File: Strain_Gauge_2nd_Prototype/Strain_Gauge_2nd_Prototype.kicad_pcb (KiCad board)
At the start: 2 copper layers, 91 parts, among them J1 TC2030, J10 2601-1104, J11 Molex_104031-0811, J2 Conn_01x04, J3 Conn_01x04, J4 Conn_01x04, J5 Conn_01x04, J6 Conn_01x04, J7 Conn_01x04, J8 Conn_01x04, J9 USB4105-GF-A-060, Q1 PMV100EPA, SW1 SW_Push, U1 ADS131M08xPBS, U2 STM32F446RETx, U3 TPS73733DCQ, U4 MCP2562-E-SN, U5 LMR33610ADDAR, U6 TPS2113APWR, Y1 7XL-8.192MBD-T

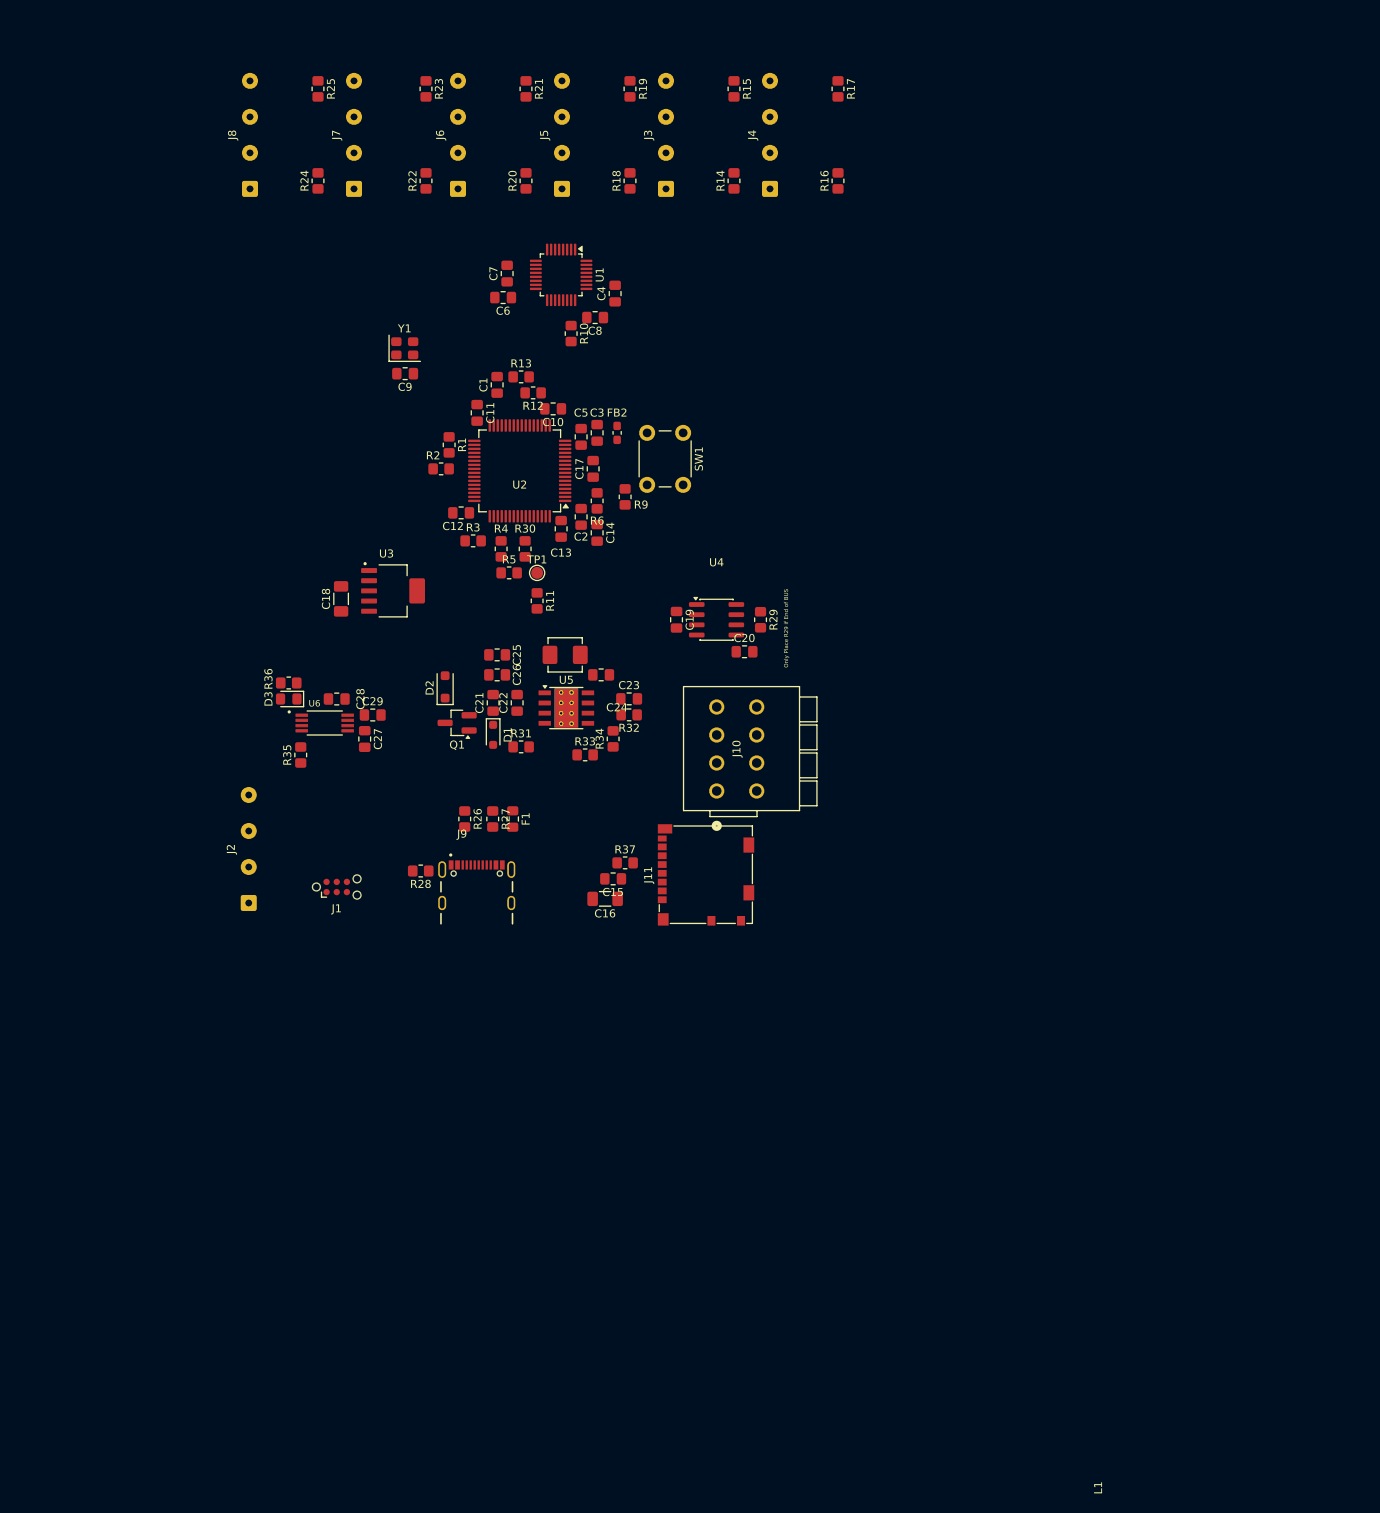
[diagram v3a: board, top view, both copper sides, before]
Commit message: Have redone the design, should be close to be routing. May just need to change the size of the 1uF capacitors down to get them closer to the ADS?
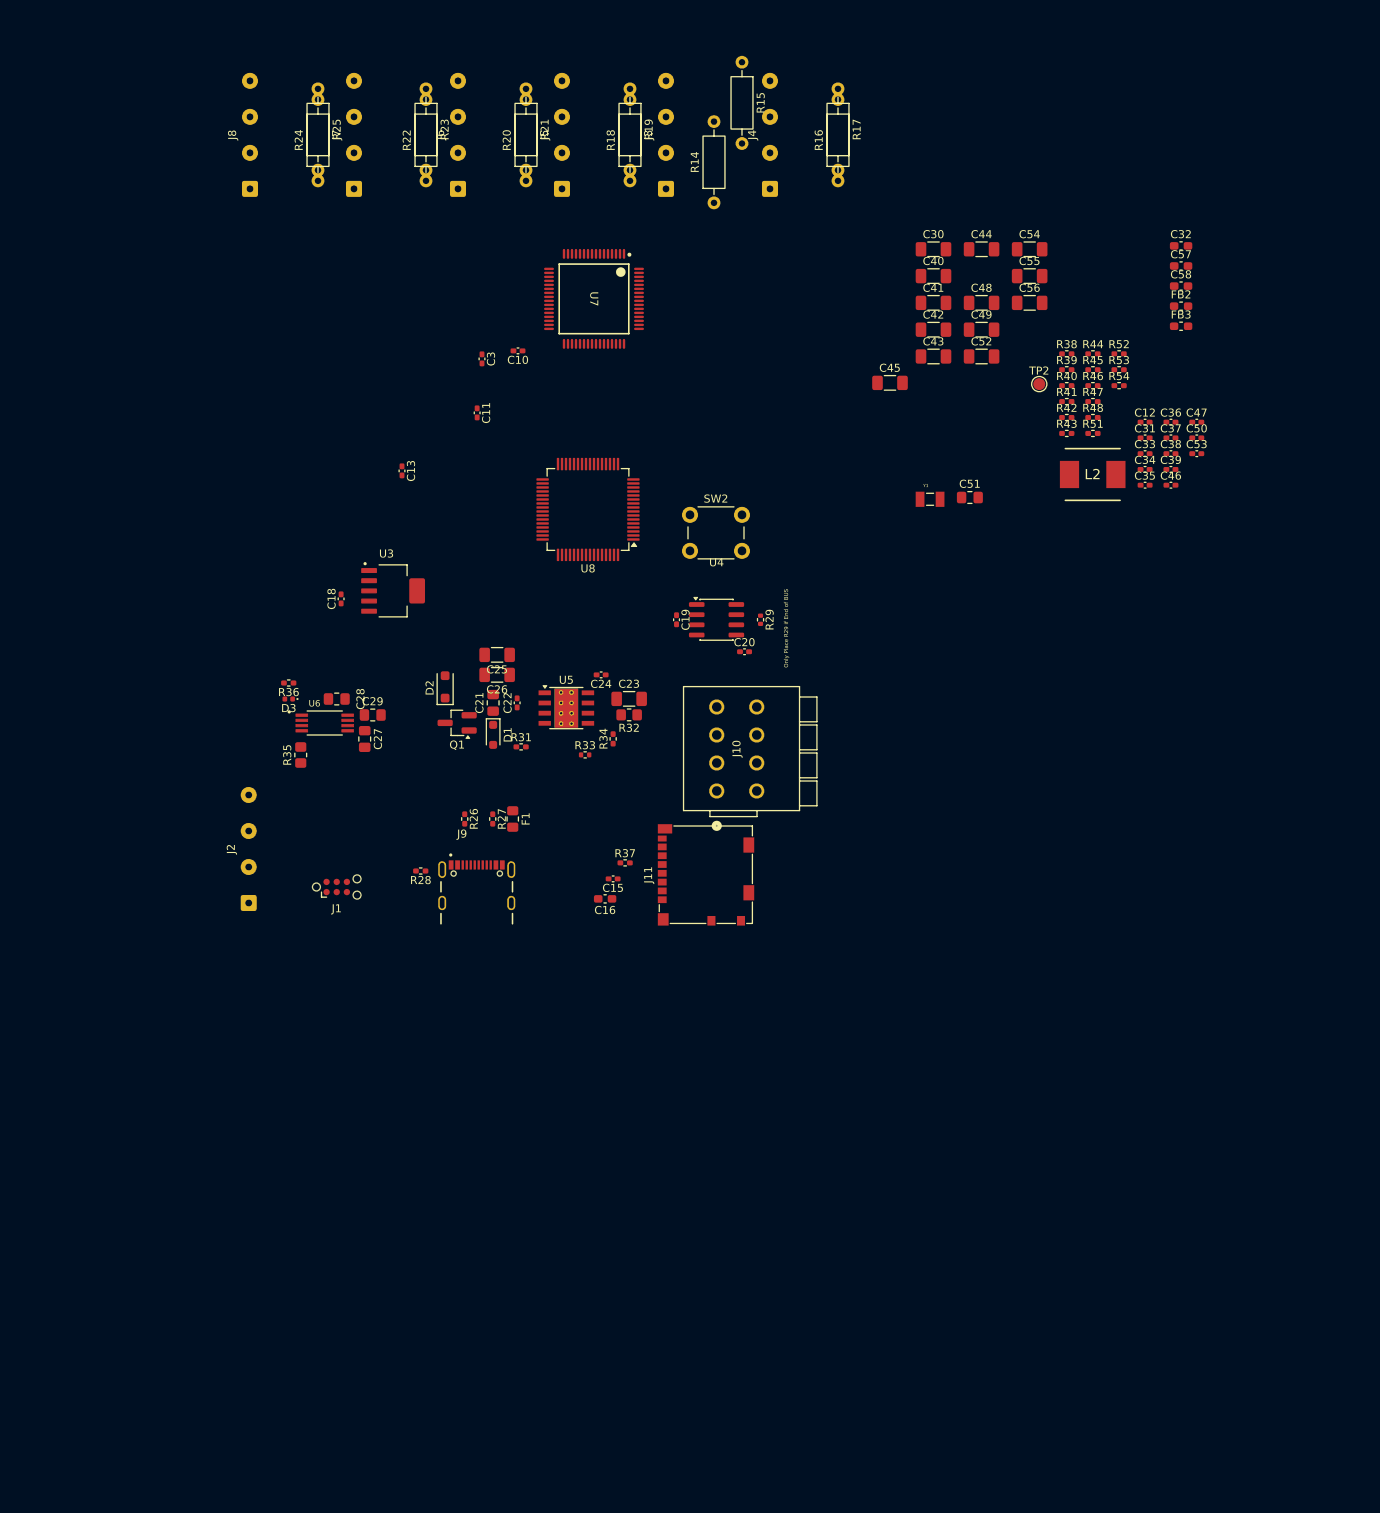
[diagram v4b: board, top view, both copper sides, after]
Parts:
- removed C1, C14: 4.7microF, Capacitor_SMD:C_0805_2012Metric_Pad1.18x1.45mm_HandSolder
- removed C17, C2, C7, C9: 100nF, Capacitor_SMD:C_0805_2012Metric_Pad1.18x1.45mm_HandSolder
- removed C4, C5, C6: 1microF, Capacitor_SMD:C_0805_2012Metric_Pad1.18x1.45mm_HandSolder
- removed C8: 220nF, Capacitor_SMD:C_0805_2012Metric_Pad1.18x1.45mm_HandSolder
- removed L1: 8.2uH, 86m, Inductor_SMD:L_Vishay_IHLP-1616
- removed R1, R11, R12, R13, R2, R3, R30, R4, R5, R6: 10k, Resistor_SMD:R_0805_2012Metric_Pad1.20x1.40mm_HandSolder
- removed R10, R9: 33, Resistor_SMD:R_0805_2012Metric_Pad1.20x1.40mm_HandSolder
- removed SW1: SW_Push, Button_Switch_THT:SW_PUSH_6mm
- removed TP1: TestPoint, TestPoint:TestPoint_Pad_D1.5mm
- removed U1: ADS131M08xPBS, Package_QFP:TQFP-32_5x5mm_P0.5mm
- removed U2: STM32F446RETx, Package_QFP:LQFP-64_10x10mm_P0.5mm
- added C30: 1microF, Capacitor_SMD:C_1206_3216Metric_Pad1.33x1.80mm_HandSolder, F.Cu at (172.9, 62.8)
- added C31: 100nF - VDDUSB, Capacitor_SMD:C_0402_1005Metric_Pad0.74x0.62mm_HandSolder, F.Cu at (199.4, 86.4)
- added C32: 4.7microF - General all board one, Capacitor_SMD:C_0603_1608Metric_Pad1.08x0.95mm_HandSolder, F.Cu at (203.9, 62.4)
- added C33: 100nF, Capacitor_SMD:C_0402_1005Metric_Pad0.74x0.62mm_HandSolder, F.Cu at (199.4, 88.3)
- added C34: 100nF, Capacitor_SMD:C_0402_1005Metric_Pad0.74x0.62mm_HandSolder, F.Cu at (199.4, 90.3)
- added C35: 100nF, Capacitor_SMD:C_0402_1005Metric_Pad0.74x0.62mm_HandSolder, F.Cu at (199.4, 92.3)
- added C36: 100nF, Capacitor_SMD:C_0402_1005Metric_Pad0.74x0.62mm_HandSolder, F.Cu at (202.6, 84.4)
- added C37: 100nF, Capacitor_SMD:C_0402_1005Metric_Pad0.74x0.62mm_HandSolder, F.Cu at (202.6, 86.4)
- added C38: 100nF, Capacitor_SMD:C_0402_1005Metric_Pad0.74x0.62mm_HandSolder, F.Cu at (202.6, 88.3)
- added C39: 100nF, Capacitor_SMD:C_0402_1005Metric_Pad0.74x0.62mm_HandSolder, F.Cu at (202.6, 90.3)
- added C40: 1microF, Capacitor_SMD:C_1206_3216Metric_Pad1.33x1.80mm_HandSolder, F.Cu at (172.9, 66.2)
- added C41: 1microF, Capacitor_SMD:C_1206_3216Metric_Pad1.33x1.80mm_HandSolder, F.Cu at (172.9, 69.5)
- added C42: 1microF, Capacitor_SMD:C_1206_3216Metric_Pad1.33x1.80mm_HandSolder, F.Cu at (172.9, 72.8)
- added C43: 1microF, Capacitor_SMD:C_1206_3216Metric_Pad1.33x1.80mm_HandSolder, F.Cu at (172.9, 76.2)
- added C44: 1microF, Capacitor_SMD:C_1206_3216Metric_Pad1.33x1.80mm_HandSolder, F.Cu at (178.9, 62.8)
- added C45: 1microF, Capacitor_SMD:C_1206_3216Metric_Pad1.33x1.80mm_HandSolder, F.Cu at (167.5, 79.5)
- added C46: 100nF, Capacitor_SMD:C_0402_1005Metric_Pad0.74x0.62mm_HandSolder, F.Cu at (202.6, 92.3)
- added C47: 100nF, Capacitor_SMD:C_0402_1005Metric_Pad0.74x0.62mm_HandSolder, F.Cu at (205.8, 84.4)
- added C48: 1microF, Capacitor_SMD:C_1206_3216Metric_Pad1.33x1.80mm_HandSolder, F.Cu at (178.9, 69.5)
- added C49: 1microF, Capacitor_SMD:C_1206_3216Metric_Pad1.33x1.80mm_HandSolder, F.Cu at (178.9, 72.8)
- added C50: 100nF, Capacitor_SMD:C_0402_1005Metric_Pad0.74x0.62mm_HandSolder, F.Cu at (205.8, 86.4)
- added C51: 10uF, Capacitor_SMD:C_0805_2012Metric_Pad1.18x1.45mm_HandSolder, F.Cu at (177.5, 93.8)
- added C52: 1microF, Capacitor_SMD:C_1206_3216Metric_Pad1.33x1.80mm_HandSolder, F.Cu at (178.9, 76.2)
- added C53: 100nF, Capacitor_SMD:C_0402_1005Metric_Pad0.74x0.62mm_HandSolder, F.Cu at (205.8, 88.3)
- added C54: 1microF, Capacitor_SMD:C_1206_3216Metric_Pad1.33x1.80mm_HandSolder, F.Cu at (185.0, 62.8)
- added C55: 1microF, Capacitor_SMD:C_1206_3216Metric_Pad1.33x1.80mm_HandSolder, F.Cu at (185.0, 66.2)
- added C56: 22uF, Capacitor_SMD:C_1206_3216Metric_Pad1.33x1.80mm_HandSolder, F.Cu at (185.0, 69.5)
- added C57: 10pF, Capacitor_SMD:C_0603_1608Metric_Pad1.08x0.95mm_HandSolder, F.Cu at (203.9, 64.9)
- added C58: 10pF, Capacitor_SMD:C_0603_1608Metric_Pad1.08x0.95mm_HandSolder, F.Cu at (203.9, 67.4)
- added FB3: 600ohm @ 100MHz,1.3A rating, 150mohm max DC resistance, Inductor_SMD:L_0603_1608Metric_Pad1.05x0.95mm_HandSolder, F.Cu at (203.9, 72.4)
- added L2: IHLP2525CZER8R2M01, Gauge Footprints:INDPM6965X300N, F.Cu at (192.8, 91.0)
- added R38: 10K, Resistor_SMD:R_0402_1005Metric_Pad0.72x0.64mm_HandSolder, F.Cu at (189.6, 75.9)
- added R39: 10K, Resistor_SMD:R_0402_1005Metric_Pad0.72x0.64mm_HandSolder, F.Cu at (189.6, 77.9)
- added R40: 10K, Resistor_SMD:R_0402_1005Metric_Pad0.72x0.64mm_HandSolder, F.Cu at (189.6, 79.8)
- added R41: 10K, Resistor_SMD:R_0402_1005Metric_Pad0.72x0.64mm_HandSolder, F.Cu at (189.6, 81.8)
- added R42: 10K, Resistor_SMD:R_0402_1005Metric_Pad0.72x0.64mm_HandSolder, F.Cu at (189.6, 83.8)
- added R43: 10K, Resistor_SMD:R_0402_1005Metric_Pad0.72x0.64mm_HandSolder, F.Cu at (189.6, 85.8)
- added R44: 10K, Resistor_SMD:R_0402_1005Metric_Pad0.72x0.64mm_HandSolder, F.Cu at (192.9, 75.9)
- added R45: 10K, Resistor_SMD:R_0402_1005Metric_Pad0.72x0.64mm_HandSolder, F.Cu at (192.9, 77.9)
- added R46: 10K, Resistor_SMD:R_0402_1005Metric_Pad0.72x0.64mm_HandSolder, F.Cu at (192.9, 79.8)
- added R47: 10K, Resistor_SMD:R_0402_1005Metric_Pad0.72x0.64mm_HandSolder, F.Cu at (192.9, 81.8)
- added R48: 10K, Resistor_SMD:R_0402_1005Metric_Pad0.72x0.64mm_HandSolder, F.Cu at (192.9, 83.8)
- added R51: 10K, Resistor_SMD:R_0402_1005Metric_Pad0.72x0.64mm_HandSolder, F.Cu at (192.9, 85.8)
- added R52: 10K, Resistor_SMD:R_0402_1005Metric_Pad0.72x0.64mm_HandSolder, F.Cu at (196.1, 75.9)
- added R53: 10K, Resistor_SMD:R_0402_1005Metric_Pad0.72x0.64mm_HandSolder, F.Cu at (196.1, 77.9)
- added R54: 10K, Resistor_SMD:R_0402_1005Metric_Pad0.72x0.64mm_HandSolder, F.Cu at (196.1, 79.8)
- added SW2: SW_Push, Button_Switch_THT:SW_PUSH_6mm, F.Cu at (142.5, 96.0)
- added TP2: TestPoint, TestPoint:TestPoint_Pad_D1.5mm, F.Cu at (186.2, 79.7)
- added U7: ADS131E08IPAG, Gauge Footprints:PAG0064A_L, F.Cu at (130.5, 69.0)
- added U8: STM32L476RGTx, Package_QFP:LQFP-64_10x10mm_P0.5mm, F.Cu at (129.8, 95.3)
- C10, C11, C12, C13, C15, C19, C20, C22, C24, C3: footprint Capacitor_SMD:C_0805_2012Metric_Pad1.18x1.45mm_HandSolder -> Capacitor_SMD:C_0402_1005Metric_Pad0.74x0.62mm_HandSolder
- C16: footprint Capacitor_SMD:C_1206_3216Metric_Pad1.33x1.80mm_HandSolder -> Capacitor_SMD:C_0603_1608Metric_Pad1.08x0.95mm_HandSolder
- C18: footprint Capacitor_SMD:C_1206_3216Metric_Pad1.33x1.80mm_HandSolder -> Capacitor_SMD:C_0402_1005Metric_Pad0.74x0.62mm_HandSolder
- C23, C25, C26: footprint Capacitor_SMD:C_0805_2012Metric_Pad1.18x1.45mm_HandSolder -> Capacitor_SMD:C_1206_3216Metric_Pad1.33x1.80mm_HandSolder
- D3: footprint Diode_SMD:D_0805_2012Metric_Pad1.15x1.40mm_HandSolder -> LED_SMD:LED_0402_1005Metric
- R14, R15, R16, R17, R18, R19, R20, R21, R22, R23, R24, R25: footprint Resistor_SMD:R_0805_2012Metric_Pad1.20x1.40mm_HandSolder -> Resistor_THT:R_Axial_DIN0207_L6.3mm_D2.5mm_P10.16mm_Horizontal
- R26, R27, R28, R31, R34, R36, R37: footprint Resistor_SMD:R_0805_2012Metric_Pad1.20x1.40mm_HandSolder -> Resistor_SMD:R_0402_1005Metric_Pad0.72x0.64mm_HandSolder
- R29, R33: footprint Resistor_SMD:R_0805_2012Metric_Pad1.20x1.40mm_HandSolder -> Resistor_SMD:R_0402_1005Metric
- Y1: value 7XL-8.192MBD-T -> ECS-.327-9-34B-TR; footprint Oscillator:Oscillator_SMD_Abracon_ASE-4Pin_3.2x2.5mm -> Gauge Footprints:XTAL_ECS-.327-9-34B-TR
- moved C12 86.2 mm to (199.4, 84.4), turned to 0 degrees
- moved FB2 72.3 mm to (203.9, 69.9), turned to 0 degrees
- moved Y1 68.3 mm to (172.5, 94.0)
- moved C13 21.2 mm to (106.5, 90.5)
- moved C3 17.1 mm to (116.5, 76.5)
- moved C10 8.48 mm to (121.0, 75.5)
- moved R14 3.72 mm to (145.5, 57.0)
- moved R15 3.48 mm to (149.0, 39.4)
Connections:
- C12 pad 1: /3.3V -> Net-(U8-VDDA)
- C13 pad 1: /3.3V -> GND
- C13 pad 2: GND -> /3.3V
- C3 pad 1: GND -> /3.3V
- C3 pad 2: Net-(U2-VDDA) -> GND
- FB2 pad 1: Net-(U2-VDDA) -> Net-(U8-VDDA)
- J11 pad 1: /DAT2 -> /SDMMC_D2
- J11 pad 2: /DAT3 -> /SDMMC_D3
- J11 pad 3: /CMD -> /SDMMC_CMD
- J11 pad 7: /DAT0 -> /SDMMC_D0
- J11 pad 8: /DAT1 -> /SDMMC_D1
- J3 pad 1: /3.3V -> /3.3VAnalog
- J4 pad 1: /3.3V -> /3.3VAnalog
- J5 pad 1: /3.3V -> /3.3VAnalog
- J6 pad 1: /3.3V -> /3.3VAnalog
- J7 pad 1: /3.3V -> /3.3VAnalog
- J8 pad 1: /3.3V -> /3.3VAnalog
- R14 pad 1: /3.3V -> /3.3VAnalog
- R16 pad 1: /3.3V -> /3.3VAnalog
- R18 pad 1: /3.3V -> /3.3VAnalog
- R20 pad 1: /3.3V -> /3.3VAnalog
- R22 pad 1: /3.3V -> /3.3VAnalog
- R24 pad 1: /3.3V -> /3.3VAnalog
- R37 pad 1: /SDCLK -> /SDMMC_CK
- Y1 pad 1: /3.3V -> /OSCIN
- Y1 pad 2: GND -> /OSCOUT
